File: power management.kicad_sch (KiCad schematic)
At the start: 32 parts, among them J1 Battery Input, J2 Charger Input, U1 LM2596T-5, U2 LM1117-3.3

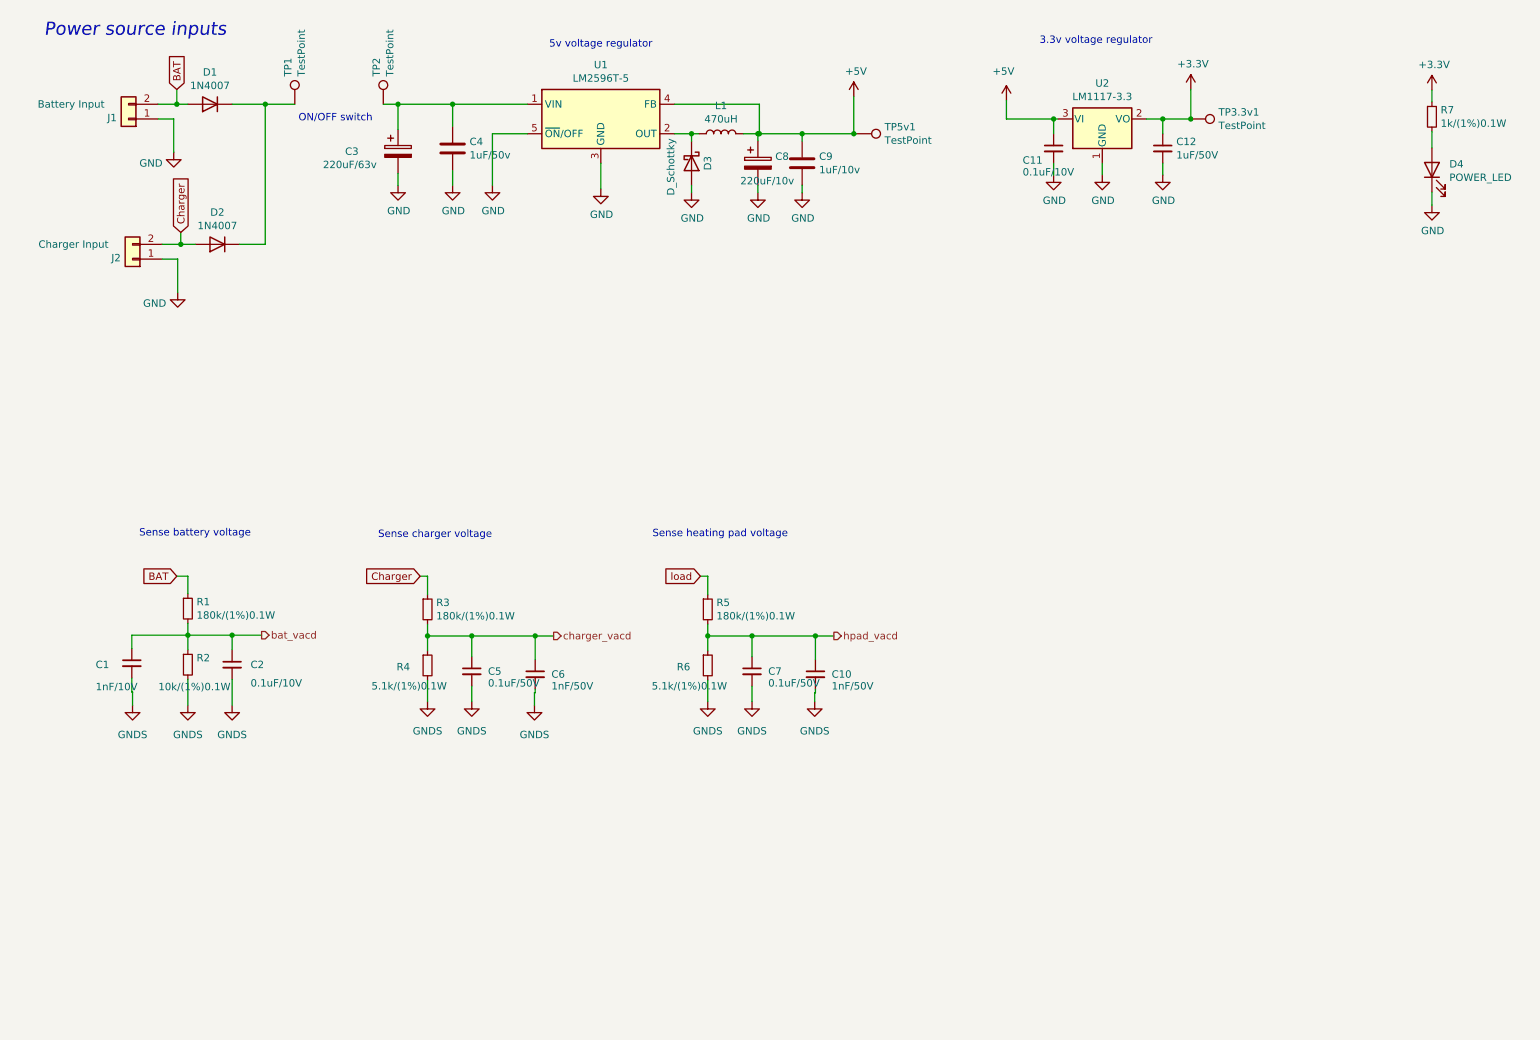
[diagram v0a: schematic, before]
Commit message: Formatted schematic and Increased power tracks
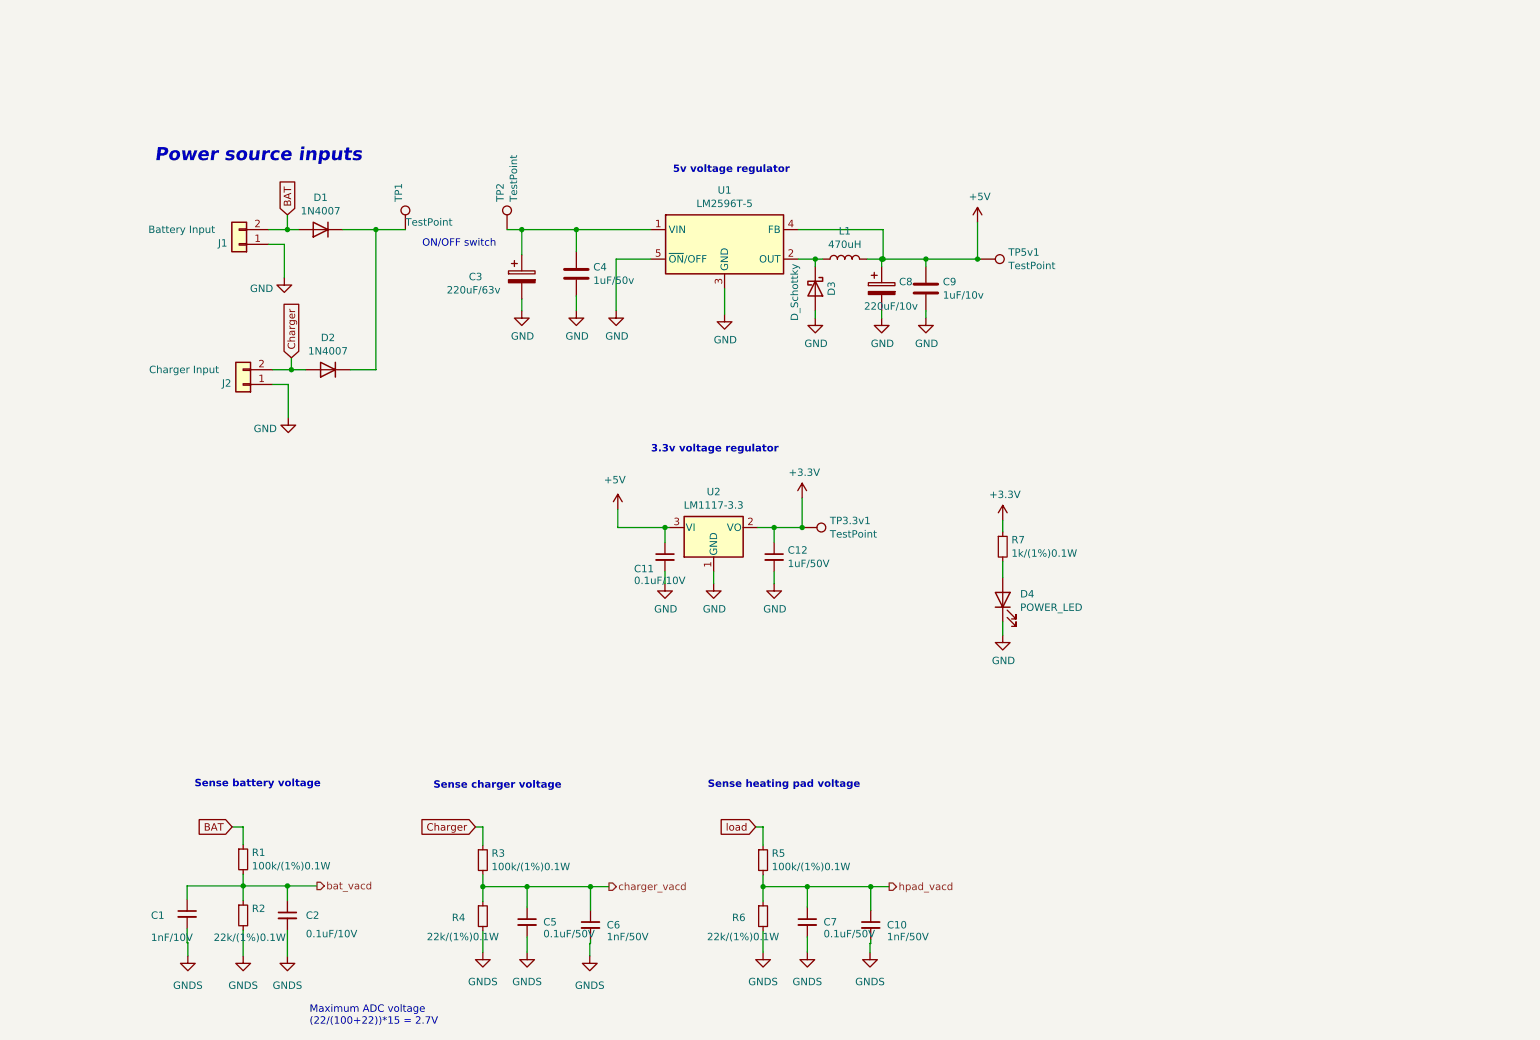
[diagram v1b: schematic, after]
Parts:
- R1, R3, R5: value 180k/(1%)0.1W -> 100k/(1%)0.1W
- R2: value 10k/(1%)0.1W -> 22k/(1%)0.1W
- R4, R6: value 5.1k/(1%)0.1W -> 22k/(1%)0.1W
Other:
- note added: "Maximum ADC voltage (22/(100+22))*15 = 2.7V"
- company: (none) -> Che innovations
- title: (none) -> Neonest v 1.3
- moved on the sheet: C1, C10, C11, C12, C2, C3, C4, C5, C6, C7, C8, C9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

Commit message: Minor changes, generated gerber files and submitted
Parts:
- removed TP1, TP2: TestPoint, TestPoint:TestPoint_Pad_D2.5mm, symbol Connector:TestPoint
- added SW1, SW2, SW3: SW_DIP_x01, Button_Switch_THT:SW_PUSH_1P1T_6x3.5mm_H5.0_APEM_MJTP1250, symbol Switch:SW_DIP_x01
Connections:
- net BAT: now also SW1.2; no longer J1.2 (Pin_2)
- net Charger: now also SW2.2; no longer J2.2 (Pin_2)
- net at C3.1, C4.1, U1.1 (VIN): now also SW3.2
- net at D1.1 (K), D2.1 (K): now also SW3.1
- new net: J1.2 (Pin_2), SW1.1
- new net: J2.2 (Pin_2), SW2.1
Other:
- note added: "Double pole double throw switch (DPDT) shall be used for total isolation"
- note added: "On/Off switch between isolates the MCU which disables the entire circuit."
- moved on the sheet: J1, J2
